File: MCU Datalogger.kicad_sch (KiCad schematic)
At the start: 25 parts, among them U1 24LC1025, U2 DS1337S+, U3 24LC1025, U4 ATMEGA328P-AU, Y1 32.768 KHz, Y2 16 MHz

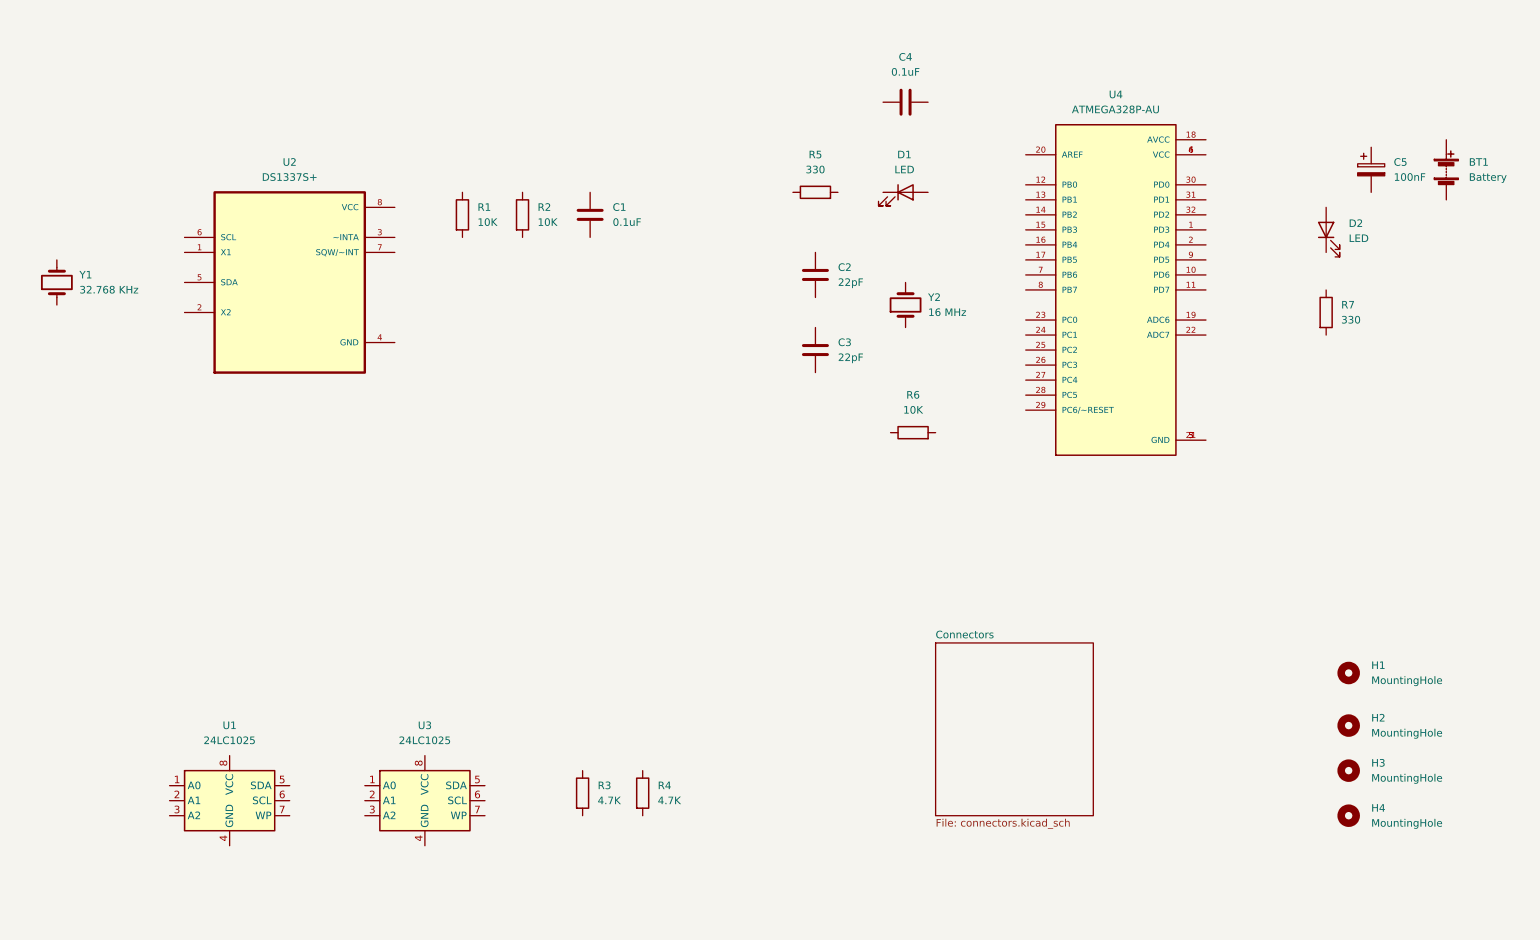
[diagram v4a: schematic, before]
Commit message: Completed wiring of main sheet.
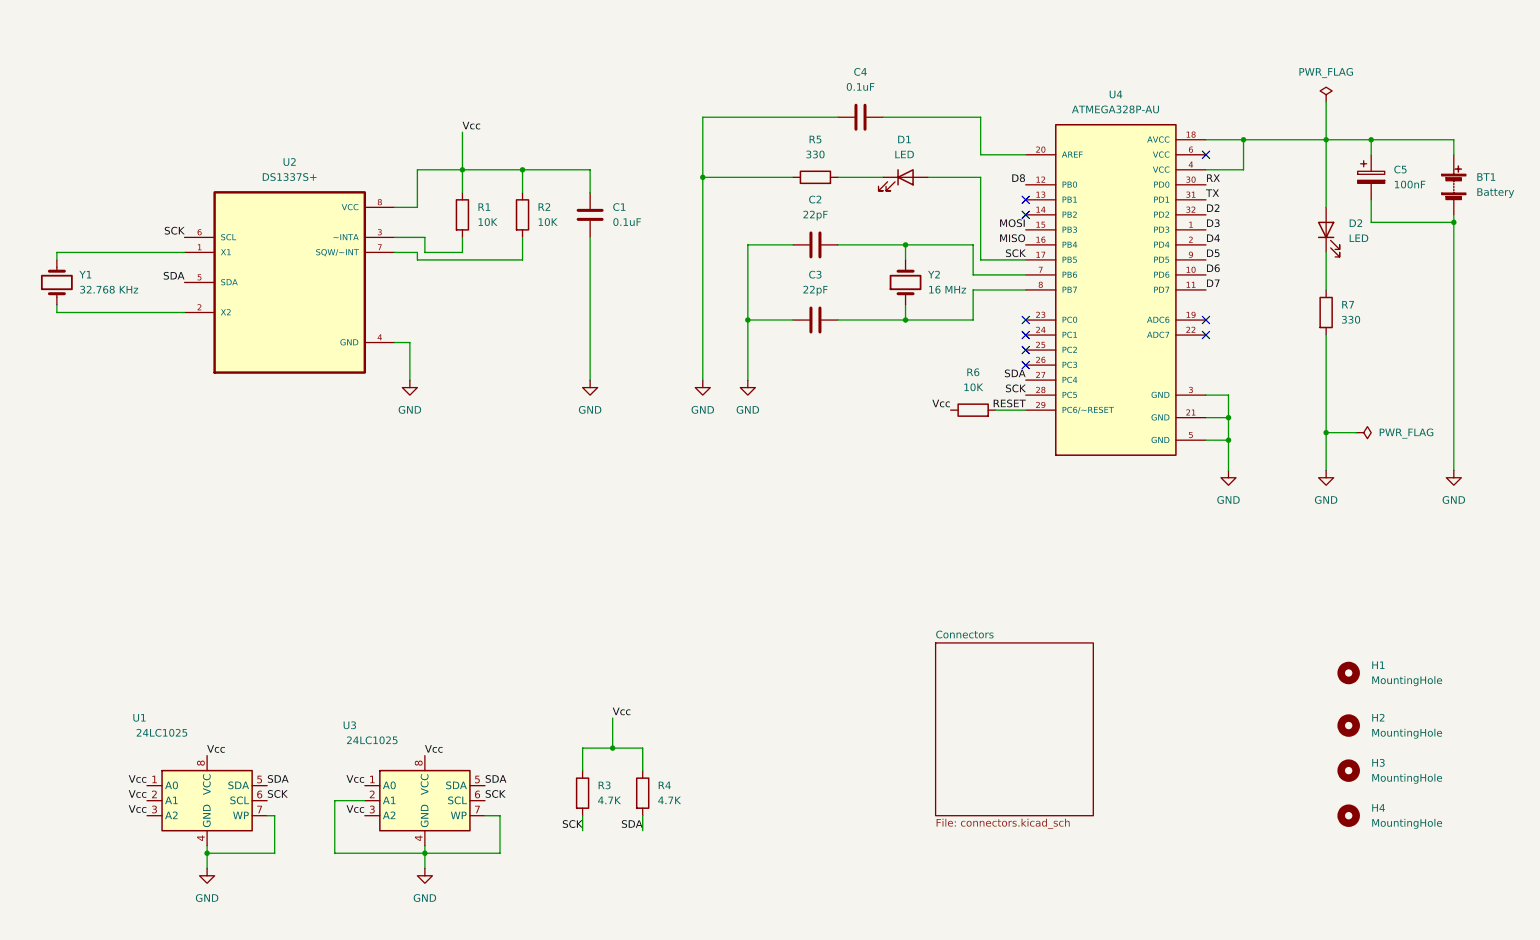
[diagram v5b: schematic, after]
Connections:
- net at R7.1: now also D2.1 (K)
- net GND: now reaches R7.2
- net GND: now also BT1.2 (-), C1.2, C2.1, C3.1, C4.1, C5.2, R5.1, U1.4 (GND), U1.7 (WP), U2.4 (GND), U3.2 (A1), U3.4 (GND), U3.7 (WP), U4.21 (GND), U4.3 (GND), U4.5 (GND)
- net at D1.1 (K): now also R5.2
- net SCK: now reaches D1.2 (A)
- net SCK: now also R3.2, U1.6 (SCL), U2.6 (SCL), U3.6 (SCL), U4.17 (PB5), U4.28 (PC5)
- net Vcc: now reaches R3.1
- net Vcc: now also C1.1, R1.1, R2.1, R4.1, R6.1, U1.1 (A0), U1.2 (A1), U1.3 (A2), U1.8 (VCC), U2.8 (VCC), U3.1 (A0), U3.3 (A2), U3.8 (VCC)
- net at U2.1 (X1): now also Y1.2
- net at U2.2 (X2): now also Y1.1
- net at U2.3 (~INTA): now also R1.2
- net SDA: now reaches U2.5 (SDA)
- net SDA: now also R4.2, U1.5 (SDA), U3.5 (SDA), U4.27 (PC4)
- net at U2.7 (SQW/~INT): now also R2.2
- net at BT1.1 (+): now also C5.1, D2.2 (A), U4.18 (AVCC), U4.4 (VCC)
- net D3: now reaches U4.1 (PD3)
- net D6: now reaches U4.10 (PD6)
- net D7: now reaches U4.11 (PD7)
- net D8: now reaches U4.12 (PB0)
- net MOSI: now reaches U4.15 (PB3)
- net MISO: now reaches U4.16 (PB4)
- net D4: now reaches U4.2 (PD4)
- net at U4.20 (AREF): now also C4.2
- net RESET: now reaches U4.29 (PC6/~RESET)
- net RESET: now also R6.2
- net RX: now reaches U4.30 (PD0)
- net TX: now reaches U4.31 (PD1)
- net D2: now reaches U4.32 (PD2)
- net at U4.6 (VCC): no longer U4.4 (VCC)
- net at U4.7 (PB6): now also C2.2, Y2.2
- net at U4.8 (PB7): now also C3.2, Y2.1
- net D5: now reaches U4.9 (PD5)
- no-connect marks 0 -> 9
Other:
- moved on the sheet: BT1, C2, C3, C4, C5, D1, R5, R6, U1, Y2

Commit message: Completed wiring in the second sheet.
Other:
- sheet Connectors ports: added D2, D3, D4, D5, D6, D7, D8, GND, MISO, MOSI, RESET, RX, SCK, SDA, TX, Vcc; removed none

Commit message: Completed comments.
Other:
- note added: "EEPROM"
- note added: "MCU"
- note added: "Mounting"
- note added: "Real time clock"
- moved on the sheet: H1, H2, H3, H4

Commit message: Fixed outstanding issues.
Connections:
- net Vcc: now also BT1.1 (+), C5.1, D2.2 (A), U4.18 (AVCC), U4.4 (VCC)
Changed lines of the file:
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@@
+    (effects (font (size 1.27 1.27)) (justify left bottom))
+  )
+  (label "Vcc" (at 255.27 38.1 0)
     (effects (font (size 1.27 1.27)) (justify left bottom))
   )
